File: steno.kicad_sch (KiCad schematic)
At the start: 16 parts, among them J1 USB_C_Receptacle_USB2.0_14P, U1 W25Q16JVSS, U2 AP2127N-3.3

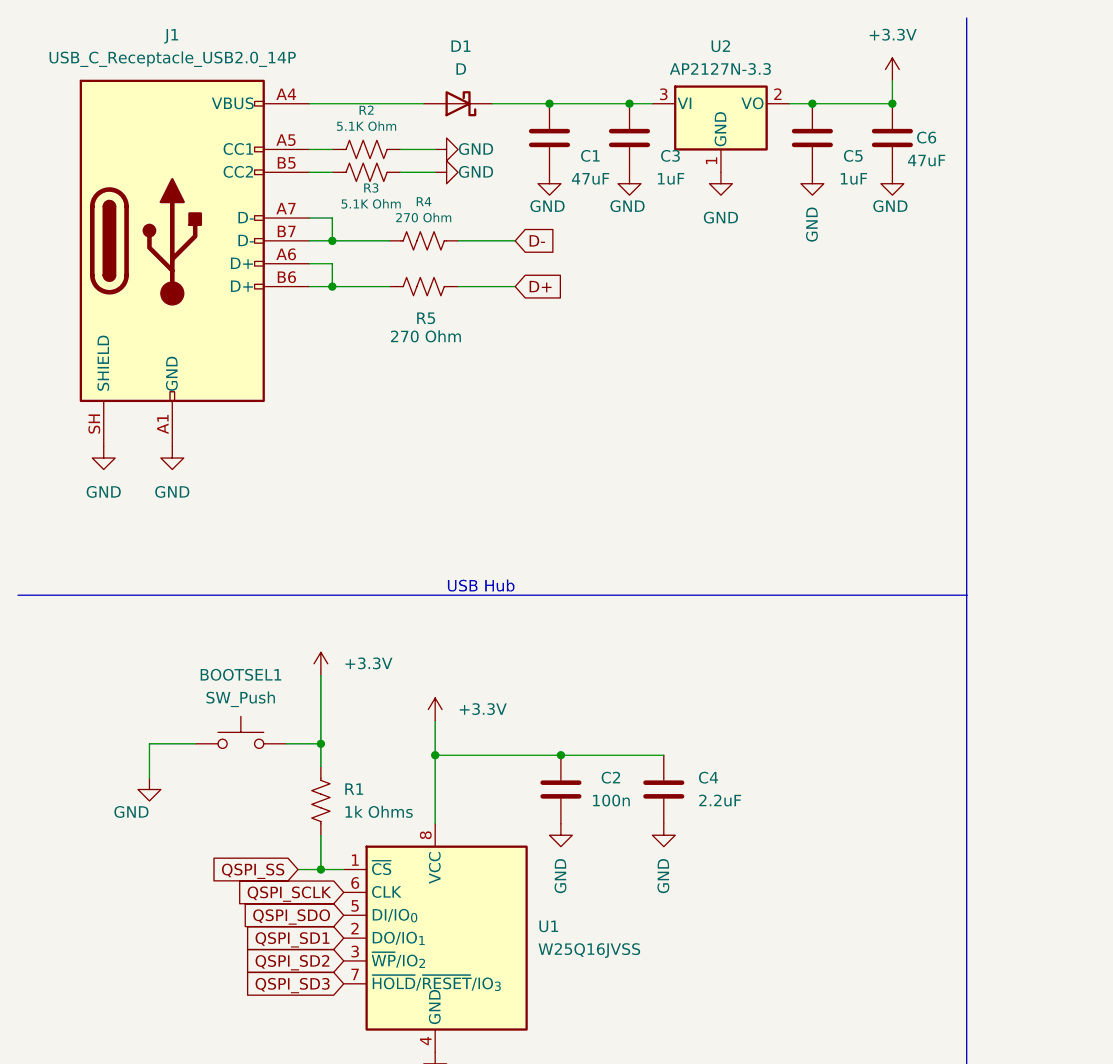
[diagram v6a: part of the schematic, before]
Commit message: Made changes based on feedback and RP2040 doc.
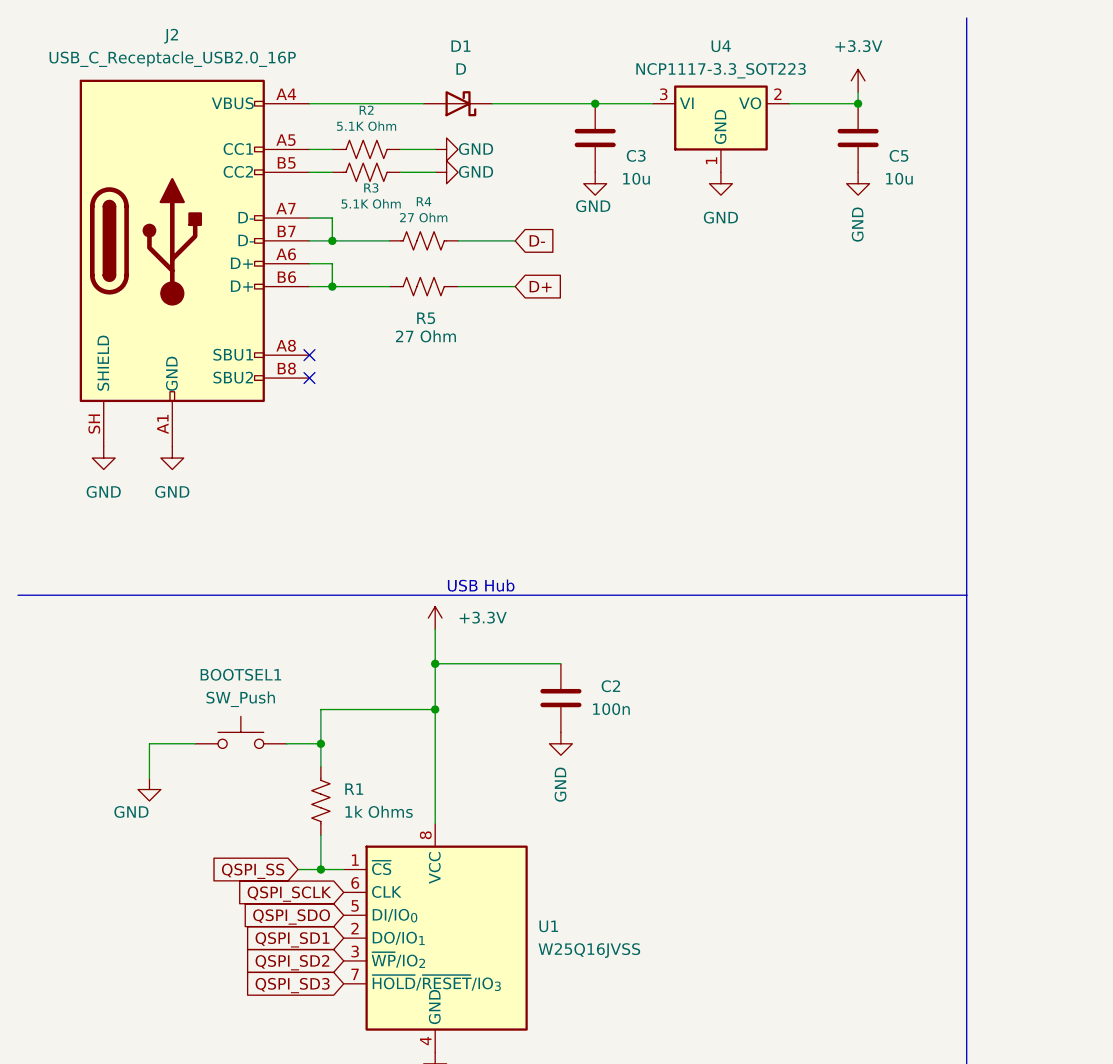
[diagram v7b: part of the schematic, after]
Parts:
- removed C1, C6: 47uF, Capacitor_SMD:C_0402_1005Metric_Pad0.74x0.62mm_HandSolder, symbol Device:C
- removed C4: 2.2uF, Capacitor_SMD:C_0402_1005Metric_Pad0.74x0.62mm_HandSolder, symbol Device:C
- removed J1: USB_C_Receptacle_USB2.0_14P, Connector_USB:USB_C_Receptacle_HRO_TYPE-C-31-M-12, symbol Connector:USB_C_Receptacle_USB2.0_14P
- removed U2: AP2127N-3.3, Package_TO_SOT_SMD:SOT-23, symbol Regulator_Linear:AP2127N-3.3
- added J2: USB_C_Receptacle_USB2.0_16P, Connector_USB:USB_C_Receptacle_HCTL_HC-TYPE-C-16P-01A, symbol Connector:USB_C_Receptacle_USB2.0_16P
- added U4: NCP1117-3.3_SOT223, Package_TO_SOT_SMD:SOT-223-3_TabPin2, symbol Regulator_Linear:NCP1117-3.3_SOT223
- C2: footprint Capacitor_SMD:C_0402_1005Metric_Pad0.74x0.62mm_HandSolder -> Capacitor_SMD:C_0402_1005Metric
- C3, C5: value 1uF -> 10u; footprint Capacitor_SMD:C_0402_1005Metric_Pad0.74x0.62mm_HandSolder -> Capacitor_SMD:C_0603_1608Metric
- D1: footprint Diode_SMD:D_SOD-323F -> Diode_SMD:D_SOD-123F
- R1, R2, R3: footprint Resistor_SMD:R_0402_1005Metric_Pad0.72x0.64mm_HandSolder -> Resistor_SMD:R_0402_1005Metric
- R4, R5: value 270 Ohm -> 27 Ohm; footprint Resistor_SMD:R_0402_1005Metric_Pad0.72x0.64mm_HandSolder -> Resistor_SMD:R_0402_1005Metric
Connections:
- net +3.3V: now also U4.2 (VO)
- net GND: now also J2.A1 (GND), J2.A12 (GND), J2.B1 (GND), J2.B12 (GND), J2.SH (SHIELD), U4.1 (GND)
- net at R2.1: now also J2.A5 (CC1)
- net at C3.1, D1.1 (K): now also U4.3 (VI)
- net at R5.1: now also J2.A6 (D+), J2.B6 (D+)
- net at R3.1: now also J2.B5 (CC2)
- net at D1.2 (A): now also J2.A4 (VBUS), J2.A9 (VBUS), J2.B4 (VBUS), J2.B9 (VBUS)
- net at R4.1: now also J2.A7 (D-), J2.B7 (D-)
- no-connect marks 0 -> 2
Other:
- moved on the sheet: C2, C3, C5

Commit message: Savepoint!
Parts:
- removed U4: NCP1117-3.3_SOT223, Package_TO_SOT_SMD:SOT-223-3_TabPin2, symbol Regulator_Linear:NCP1117-3.3_SOT223
- added U2: AMS1117-3.3, Package_TO_SOT_SMD:SOT-223-3_TabPin2, symbol Regulator_Linear:AMS1117-3.3
- D1: footprint Diode_SMD:D_SOD-123F -> Diode_SMD:D_SMA
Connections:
- net +3.3V: now also U2.2 (VO); no longer BOOTSEL1.2
- net GND: now also U2.1 (GND)
- net QSPI_SS: now also BOOTSEL1.2
- net at C3.1, D1.1 (K): now also U2.3 (VI)
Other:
- moved on the sheet: BOOTSEL1, R1
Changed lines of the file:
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@@
-	)
-	(junction
-		(at 45.72 92.71)
-		(diameter 0)
-		(color 0 0 0 0)
 	)
 	(junction
@@
 	)
 	(junction
+		(at 45.72 100.33)
+		(diameter 0)
+		(color 0 0 0 0)
+	)
+	(junction
 		(at 45.72 106.68)
 		(diameter 0)
@@
 	(wire
 		(pts
-			(xy 41.91 92.71) (xy 45.72 92.71)
+			(xy 41.91 100.33) (xy 45.72 100.33)
 		)
 		(stroke
@@
 	(wire
 		(pts
-			(xy 45.72 92.71) (xy 45.72 95.25)
-		)
-		(stroke
-			(width 0)
-			(type default)
-		)
-	)
-	(wire
-		(pts
 			(xy 105.41 20.32) (xy 105.41 21.59)
 		)
@@
 	(wire
 		(pts
+			(xy 45.72 97.79) (xy 45.72 100.33)
+		)
+		(stroke
+			(width 0)
+			(type default)
+		)
+	)
+	(wire
+		(pts
 			(xy 43.18 106.68) (xy 45.72 106.68)
 		)
@@
 	(wire
 		(pts
+			(xy 45.72 100.33) (xy 45.72 106.68)
+		)
+		(stroke
+			(width 0)
+			(type default)
+		)
+	)
+	(wire
+		(pts
 			(xy 60.96 36.83) (xy 67.31 36.83)
 		)
@@
 	(wire
 		(pts
+			(xy 30.48 100.33) (xy 30.48 101.6)
+		)
+		(stroke
+			(width 0)
+			(type default)
+		)
+	)
+	(wire
+		(pts
 			(xy 45.72 106.68) (xy 48.26 106.68)
 		)
@@
 	(wire
 		(pts
-			(xy 26.67 92.71) (xy 31.75 92.71)
+			(xy 30.48 100.33) (xy 31.75 100.33)
 		)
 		(stroke
@@
 	(wire
 		(pts
-			(xy 26.67 92.71) (xy 26.67 96.52)
-		)
-		(stroke
-			(width 0)
-			(type default)
-		)
-	)
-	(wire
-		(pts
 			(xy 58.42 80.01) (xy 58.42 83.82)
 		)
@@
 	(wire
 		(pts
-			(xy 45.72 102.87) (xy 45.72 106.68)
-		)
-		(stroke
-			(width 0)
-			(type default)
-		)
-	)
-	(wire
-		(pts
-			(xy 45.72 88.9) (xy 45.72 92.71)
+			(xy 45.72 88.9) (xy 45.72 90.17)
 		)
 		(stroke
@@
 	)
 	(symbol
+		(lib_id "Regulator_Linear:AMS1117-3.3")
+		(at 90.17 21.59 0)
+		(unit 1)
+		(body_style 1)
+		(exclude_from_sim no)
+		(in_bom yes)
+		(on_board yes)
+		(in_pos_files yes)
+		(dnp no)
+		(fields_autoplaced yes)
+		(property "Reference" "U2"
+			(at 90.17 15.24 0)
+			(show_name no)
+			(do_not_autoplace no)
+			(effects
+				(font
+					(size 1.27 1.27)
+				)
+			)
+		)
+		(property "Value" "AMS1117-3.3"
+			(at 90.17 17.78 0)
+			(show_name no)
+			(do_not_autoplace no)
+			(effects
+				(font
+					(size 1.27 1.27)
+				)
+			)
+		)
+		(property "Footprint" "Package_TO_SOT_SMD:SOT-223-3_TabPin2"
+			(at 90.17 16.51 0)
+			(hide yes)
+			(show_name no)
+			(do_not_autoplace no)
+			(effects
+				(font
+					(size 1.27 1.27)
+				)
+			)
+		)
+		(property "Datasheet" "http://www.advanced-monolithic.com/pdf/ds1117.pdf"
+			(at 92.71 27.94 0)
+			(hide yes)
+			(show_name no)
+			(do_not_autoplace no)
+			(effects
+				(font
+					(size 1.27 1.27)
+				)
+			)
+		)
+		(property "Description" "1A Low Dropout regulator, positive, 3.3V fixed output, SOT-223"
+			(at 90.17 21.59 0)
+			(hide yes)
+			(show_name no)
+			(do_not_autoplace no)
+			(effects
+				(font
+					(size 1.27 1.27)
+				)
+			)
+		)
+		(pin "2"
+		)
+		(pin "1"
+		)
+		(pin "3"
+		)
+		(instances
+			(project "steno"
+				(path "/238e1d3b-9ec5-448b-85c7-386a29cd2631"
+					(reference "U2")
+					(unit 1)
+				)
+			)
+		)
+	)
+	(symbol
 		(lib_id "Device:R_US")
 		(at 50.8 26.67 90)
@@
 	(symbol
 		(lib_id "power:GND")
-		(at 26.67 96.52 0)
+		(at 30.48 101.6 0)
 		(unit 1)
 		(body_style 1)
@@
 		(dnp no)
 		(property "Reference" "#PWR02"
-			(at 26.67 102.87 0)
+			(at 30.48 107.95 0)
 			(hide yes)
 			(show_name no)
@@
 		)
 		(property "Value" "GND"
-			(at 26.6701 100.33 0)
+			(at 30.4801 105.41 0)
 			(show_name no)
 			(do_not_autoplace no)
@@
 		)
 		(property "Footprint" ""
-			(at 26.67 96.52 0)
+			(at 30.48 101.6 0)
 			(hide yes)
 			(show_name no)
@@
 		)
 		(property "Datasheet" ""
-			(at 26.67 96.52 0)
+			(at 30.48 101.6 0)
 			(hide yes)
 			(show_name no)
@@
 		)
 		(property "Description" "Power symbol creates a global label with name \"GND\" , ground"
-			(at 26.67 96.52 0)
+			(at 30.48 101.6 0)
 			(hide yes)
 			(show_name no)
@@
 				(path "/238e1d3b-9ec5-448b-85c7-386a29cd2631"
 					(reference "R3")
-					(unit 1)
-				)
-			)
-		)
-	)
-	(symbol
-		(lib_id "Regulator_Linear:NCP1117-3.3_SOT223")
-		(at 90.17 21.59 0)
-		(unit 1)
-		(body_style 1)
-		(exclude_from_sim no)
-		(in_bom yes)
-		(on_board yes)
-		(in_pos_files yes)
-		(dnp no)
-		(fields_autoplaced yes)
-		(property "Reference" "U4"
-			(at 90.17 15.24 0)
-			(show_name no)
-			(do_not_autoplace no)
-			(effects
-				(font
-					(size 1.27 1.27)
-				)
-			)
-		)
-		(property "Value" "NCP1117-3.3_SOT223"
-			(at 90.17 17.78 0)
-			(show_name no)
-			(do_not_autoplace no)
-			(effects
-				(font
-					(size 1.27 1.27)
-				)
-			)
-		)
-		(property "Footprint" "Package_TO_SOT_SMD:SOT-223-3_TabPin2"
-			(at 90.17 16.51 0)
-			(hide yes)
-			(show_name no)
-			(do_not_autoplace no)
-			(effects
-				(font
-					(size 1.27 1.27)
-				)
-			)
-		)
-		(property "Datasheet" "http://www.onsemi.com/pub_link/Collateral/NCP1117-D.PDF"
-			(at 92.71 27.94 0)
-			(hide yes)
-			(show_name no)
-			(do_not_autoplace no)
-			(effects
-				(font
-					(size 1.27 1.27)
-				)
-			)
-		)
-		(property "Description" "1A Low drop-out regulator, Fixed Output 3.3V, SOT-223"
-			(at 90.17 21.59 0)
-			(hide yes)
-			(show_name no)
-			(do_not_autoplace no)
-			(effects
-				(font
-					(size 1.27 1.27)
-				)
-			)
-		)
-		(pin "1"
-		)
-		(pin "2"
-		)
-		(pin "3"
-		)
-		(instances
-			(project "steno"
-				(path "/238e1d3b-9ec5-448b-85c7-386a29cd2631"
-					(reference "U4")
 					(unit 1)
 				)
@@
 			)
 		)
-		(property "Footprint" "Diode_SMD:D_SOD-123F"
+		(property "Footprint" "Diode_SMD:D_SMA"
 			(at 60.96 21.59 0)
 			(hide yes)
@@
 	(symbol
 		(lib_id "Device:R_US")
-		(at 45.72 99.06 0)
+		(at 45.72 93.98 0)
 		(unit 1)
 		(body_style 1)
@@
 		(fields_autoplaced yes)
 		(property "Reference" "R1"
-			(at 48.26 97.7899 0)
+			(at 48.26 92.7099 0)
 			(show_name no)
 			(do_not_autoplace no)
@@
 		)
 		(property "Value" "1k Ohms"
-			(at 48.26 100.3299 0)
+			(at 48.26 95.2499 0)
 			(show_name no)
 			(do_not_autoplace no)
@@
 		)
 		(property "Footprint" "Resistor_SMD:R_0402_1005Metric"
-			(at 46.736 99.314 90)
+			(at 46.736 94.234 90)
 			(hide yes)
 			(show_name no)
@@
 		)
 		(property "Datasheet" ""
-			(at 45.72 99.06 0)
+			(at 45.72 93.98 0)
 			(hide yes)
 			(show_name no)
@@
 		)
 		(property "Description" "Resistor, US symbol"
-			(at 45.72 99.06 0)
+			(at 45.72 93.98 0)
 			(hide yes)
 			(show_name no)
@@
 	(symbol
 		(lib_id "Switch:SW_Push")
-		(at 36.83 92.71 0)
+		(at 36.83 100.33 0)
 		(unit 1)
 		(body_style 1)
@@
 		(fields_autoplaced yes)
 		(property "Reference" "BOOTSEL1"
-			(at 36.83 85.09 0)
+			(at 36.83 92.71 0)
 			(show_name no)
 			(do_not_autoplace no)
@@
 		)
 		(property "Value" "SW_Push"
-			(at 36.83 87.63 0)
+			(at 36.83 95.25 0)
 			(show_name no)
 			(do_not_autoplace no)
@@
 		)
 		(property "Footprint" "3rd_party_footprints:SW4_PTS815 SJM 250 SMTR LFS_CNK"
-			(at 36.83 87.63 0)
+			(at 36.83 95.25 0)
 			(hide yes)
 			(show_name no)
@@
 		)
 		(property "Datasheet" ""
-			(at 36.83 87.63 0)
+			(at 36.83 95.25 0)
 			(hide yes)
 			(show_name no)
@@
 		)
 		(property "Description" "Push button switch, generic, two pins"
-			(at 36.83 92.71 0)
-			(hide yes)
-			(show_name no)
+			(at 36.83 100.33 0)
+			(hide yes)
+			(show_name no)
